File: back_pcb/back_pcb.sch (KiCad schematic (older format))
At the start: 79 parts, among them J1 Conn_01x12, P2 EXPANSION_BOTTOM, P3 EXPANSION_TOP, P4 AUDIO_CONN, P6 ATMEGA_HEADER, P7 EXPANSION_BOTTOM2, P8 JST, P9 USB_A, Q1 IRLML6401, Q2 IRLML6401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

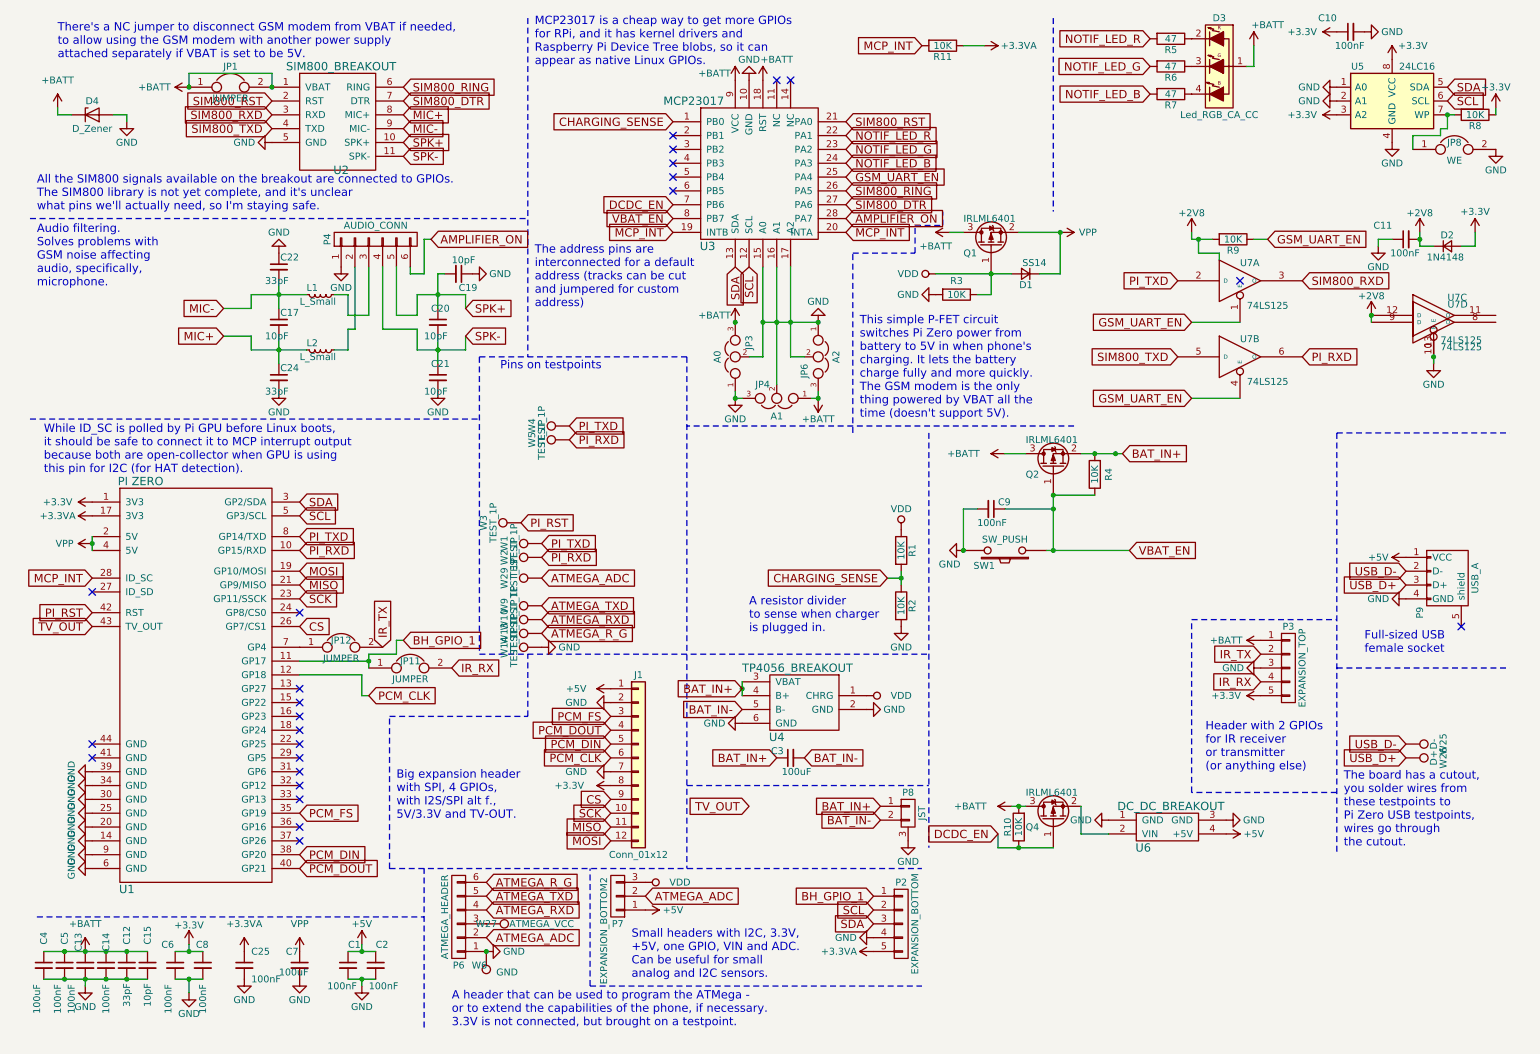
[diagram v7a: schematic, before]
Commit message: Added LM339 - monitoring charger and 5V stepup undervoltage
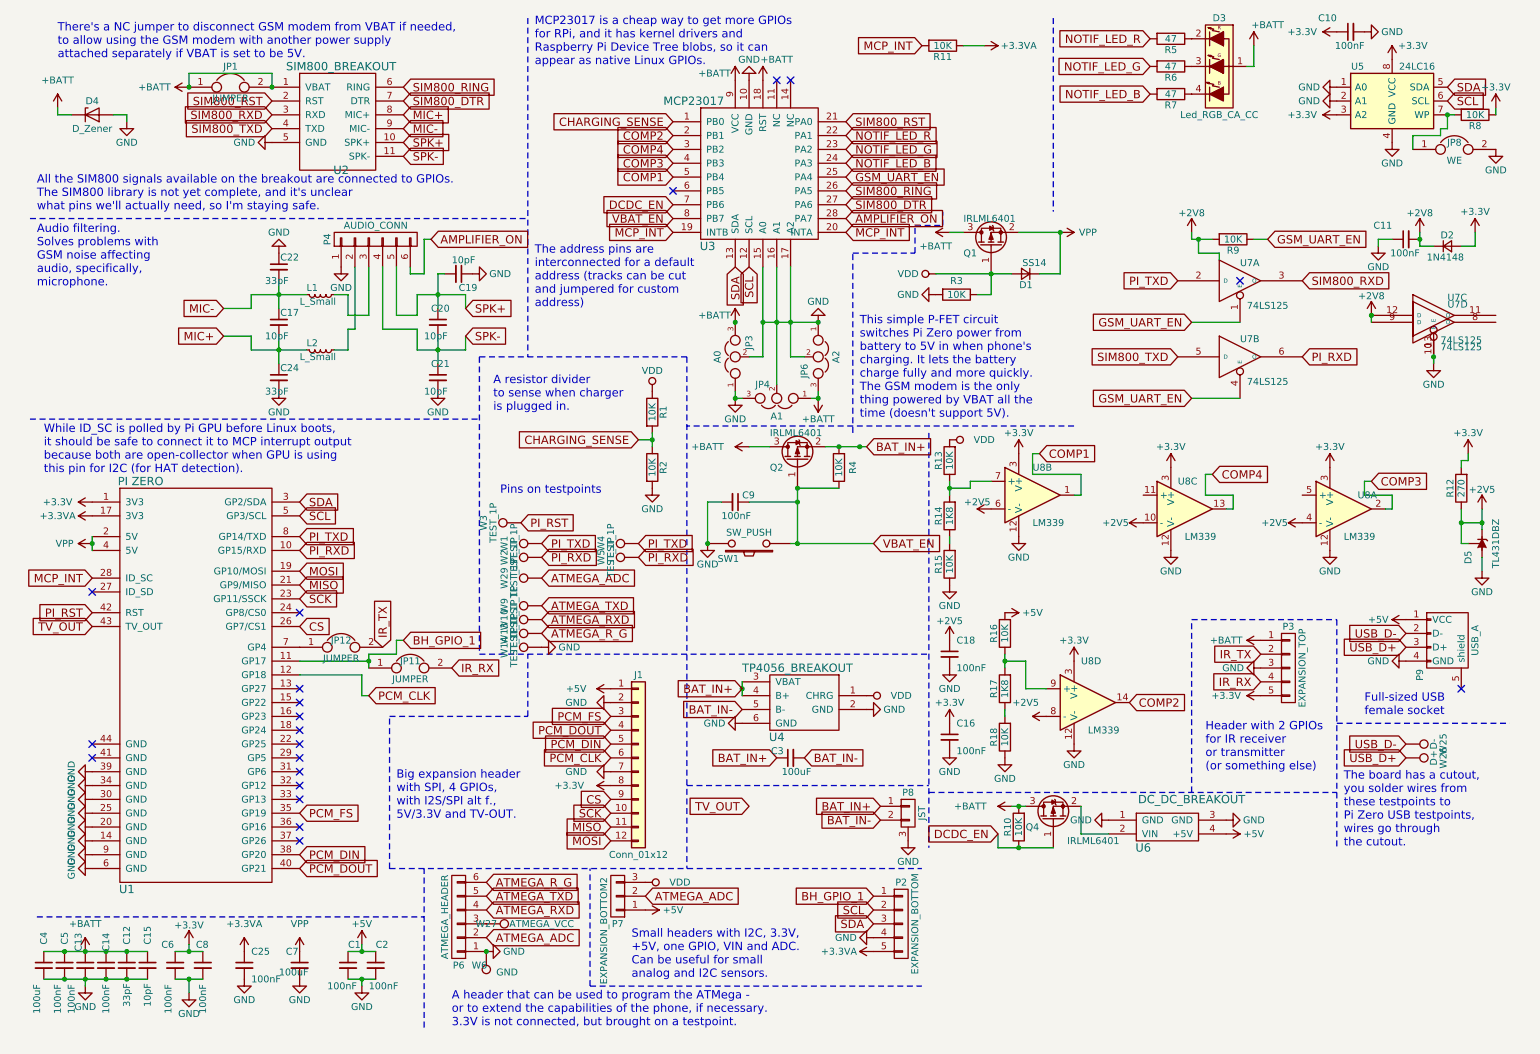
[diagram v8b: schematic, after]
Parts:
- added C16, C18: 100nF, common-footprints:C_0805_100nF_HandSoldering, symbol C_Small
- added D5: TL431DBZ, TO_SOT_Packages_SMD:SOT-23, symbol TL431DBZ
- added R12: 270, Resistors_SMD:R_0603_HandSoldering, symbol R
- added R13, R15, R16, R18: 10K, common-footprints:R_0805_10K_HandSoldering, symbol R
- added R14, R17: 1K8, Resistors_SMD:R_0603_HandSoldering, symbol R
- added U8: LM339, Housings_SOIC:SOIC-14_3.9x8.7mm_Pitch1.27mm, symbol LM339
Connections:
- net +3V3: now also C16.1, R12.2, U8.3 (V+), U8.3 (V+), U8.3 (V+), U8.3 (V+)
- net +5V: now also R16.2
- net GND: now also C16.2, C18.2, D5.3 (A), R15.1, R18.1, U8.12 (V-), U8.12 (V-), U8.12 (V-), U8.12 (V-)
- net VDD: now also R13.2
- net COMP2: now reaches U3.2 (PB1)
- net COMP2: now also U8.14
- net COMP4: now reaches U3.3 (PB2)
- net COMP4: now also U8.13
- net COMP3: now reaches U3.4 (PB3)
- net COMP3: now also U8.2
- net COMP1: now reaches U3.5 (PB4)
- net COMP1: now also U8.1
- new net: R13.1, R14.2, U8.7 (+)
- new net: R16.1, R17.2, U8.9 (+)
- new net: R14.1, R15.2
- new net: R17.1, R18.2
- new net +2V5: C18.1, D5.1 (K), D5.2 (REF), R12.1, U8.10 (-), U8.4 (-), U8.6 (-), U8.8 (-)
- no-connect marks 24 -> 20
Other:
- note added: "Header with 2 GPIOs\nfor IR receiver \nor transmitter\n(or something else)"
- note removed: "Header with 2 GPIOs\nfor IR receiver \nor transmitter\n(or anything else)"
- moved on the sheet: C9, P9, Q2, R1, R2, R4, SW1, W4, W5
